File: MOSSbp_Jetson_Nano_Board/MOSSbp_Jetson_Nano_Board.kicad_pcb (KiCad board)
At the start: 2 copper layers, 0 parts

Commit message: Started PCB design
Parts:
- added C1: 4.7u, Capacitor_SMD:C_1206_3216Metric_Pad1.42x1.75mm_HandSolder, F.Cu at (122.5, 98.3)
- added C10: 4.7u, Capacitor_SMD:C_1206_3216Metric_Pad1.42x1.75mm_HandSolder, F.Cu at (132.2, 98.2)
- added C11: 2.2u, Capacitor_SMD:C_0603_1608Metric_Pad1.05x0.95mm_HandSolder, F.Cu at (169.0, 114.0)
- added C12: 0.1u, Capacitor_SMD:C_0603_1608Metric_Pad1.05x0.95mm_HandSolder, F.Cu at (129.4, 95.5)
- added C13: 330u, Capacitor_SMD:CP_Elec_8x10, F.Cu at (166.2, 69.0)
- added C2: 4.7u, Capacitor_SMD:C_1206_3216Metric_Pad1.42x1.75mm_HandSolder, F.Cu at (144.0, 98.5)
- added C3: 220u, Capacitor_SMD:CP_Elec_8x10.5, F.Cu at (125.0, 81.4)
- added C4: 10u, Capacitor_SMD:C_1206_3216Metric_Pad1.42x1.75mm_HandSolder, F.Cu at (131.4, 81.4)
- added C5: 0.1u, Capacitor_SMD:C_0603_1608Metric_Pad1.05x0.95mm_HandSolder, F.Cu at (119.6, 95.2)
- added C6: 0.1u, Capacitor_SMD:C_0603_1608Metric_Pad1.05x0.95mm_HandSolder, F.Cu at (140.9, 95.8)
- added C7: 22n, Capacitor_SMD:C_0603_1608Metric_Pad1.05x0.95mm_HandSolder, F.Cu at (141.6, 79.7)
- added C8: 0.1u, Capacitor_SMD:C_0603_1608Metric_Pad1.05x0.95mm_HandSolder, F.Cu at (136.2, 76.3)
- added C9: 47u, Capacitor_SMD:C_2220_5650Metric_Pad1.97x5.40mm_HandSolder, F.Cu at (135.2, 90.2)
- added D1: D, Diode_SMD:D_SOD-123, F.Cu at (119.3, 110.5)
- added D2: D, Diode_SMD:D_SOD-123, F.Cu at (133.7, 110.5)
- added D3: PMEG4030EP, Diode_SMD:D_SOD-128, F.Cu at (144.1, 79.8)
- added D4: D, Diode_SMD:D_SOD-123, F.Cu at (126.7, 110.5)
- added J1: 24V, TerminalBlock_Phoenix:TerminalBlock_Phoenix_MKDS-1,5-2_1x02_P5.00mm_Horizontal, F.Cu at (138.0, 68.2)
- added J2: Circulation Fan, Connector_JST:JST_GH_BM02B-GHS-TBT_1x02-1MP_P1.25mm_Vertical, F.Cu at (119.5, 115.1)
- added J3: CO2, Connector_JST:JST_GH_BM02B-GHS-TBT_1x02-1MP_P1.25mm_Vertical, F.Cu at (133.5, 115.1)
- added J4: Water Pump PWM, Connector_JST:JST_GH_BM02B-GHS-TBT_1x02-1MP_P1.25mm_Vertical, F.Cu at (140.5, 115.1)
- added J5: Vent Fan, Connector_JST:JST_GH_BM02B-GHS-TBT_1x02-1MP_P1.25mm_Vertical, F.Cu at (126.5, 115.1)
- added J6: Water Pump, Connector_JST:JST_XH_B2B-XH-AM_1x02_P2.50mm_Vertical, F.Cu at (145.5, 68.8)
- added J7: I2C, Connector_JST:JST_GH_BM04B-GHS-TBT_1x04-1MP_P1.25mm_Vertical, F.Cu at (156.3, 70.4)
- added J8: Jetson_Nano_Dev, Connector_PinHeader_2.54mm:PinHeader_2x20_P2.54mm_Vertical, F.Cu at (174.5, 68.7)
- added L1: 8.2u, RG_footprints:SRN8040-8R2Y, F.Cu at (142.5, 90.2)
- added Q1: DMN3404L, Package_TO_SOT_SMD:SOT-23, F.Cu at (119.5, 103.5)
- added Q2: DMN3404L, Package_TO_SOT_SMD:SOT-23, F.Cu at (141.2, 104.0)
- added Q3: BSS138, Package_TO_SOT_SMD:SOT-23, F.Cu at (143.1, 109.0)
- added Q4: DMN3404L, Package_TO_SOT_SMD:SOT-23, F.Cu at (129.2, 103.8)
- added R1: 23.7k, Resistor_SMD:R_0603_1608Metric_Pad1.05x0.95mm_HandSolder, F.Cu at (136.2, 83.9)
- added R10: 4.7k, Resistor_SMD:R_0603_1608Metric_Pad1.05x0.95mm_HandSolder, F.Cu at (139.0, 109.0)
- added R2: 4.7k, Resistor_SMD:R_0603_1608Metric_Pad1.05x0.95mm_HandSolder, F.Cu at (117.0, 98.1)
- added R3: 4.7k, Resistor_SMD:R_0603_1608Metric_Pad1.05x0.95mm_HandSolder, F.Cu at (137.8, 98.8)
- added R4: 100k, Resistor_SMD:R_0603_1608Metric_Pad1.05x0.95mm_HandSolder, F.Cu at (130.1, 88.6)
- added R5: 6.49k, Resistor_SMD:R_0603_1608Metric_Pad1.05x0.95mm_HandSolder, F.Cu at (130.1, 91.9)
- added R6: 10k, Resistor_SMD:R_0603_1608Metric_Pad1.05x0.95mm_HandSolder, F.Cu at (145.5, 109.1)
- added R7: 10k, Resistor_SMD:R_0603_1608Metric_Pad1.05x0.95mm_HandSolder, F.Cu at (140.5, 109.1)
- added R8: 4.7k, Resistor_SMD:R_0603_1608Metric_Pad1.05x0.95mm_HandSolder, F.Cu at (126.5, 98.4)
- added R9: 21k, Resistor_SMD:R_0603_1608Metric_Pad1.05x0.95mm_HandSolder, F.Cu at (165.1, 114.0)
- added U1: MIC4416, Package_TO_SOT_SMD:SOT-143, F.Cu at (119.5, 98.2)
- added U2: MIC4416, Package_TO_SOT_SMD:SOT-143, F.Cu at (140.8, 98.7)
- added U3: LMR14020, Package_SO:SOIC-8-1EP_3.9x4.9mm_P1.27mm_EP2.41x3.3mm, F.Cu at (136.5, 80.1)
- added U4: PTN78020WAH, RG_footprints:PTN78020WAH, F.Cu at (160.4, 94.5)
- added U5: MIC4416, Package_TO_SOT_SMD:SOT-143, F.Cu at (129.2, 98.5)
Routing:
- added copper zone on B.Cu, net GND
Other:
- board outline added: 65 x 60 mm

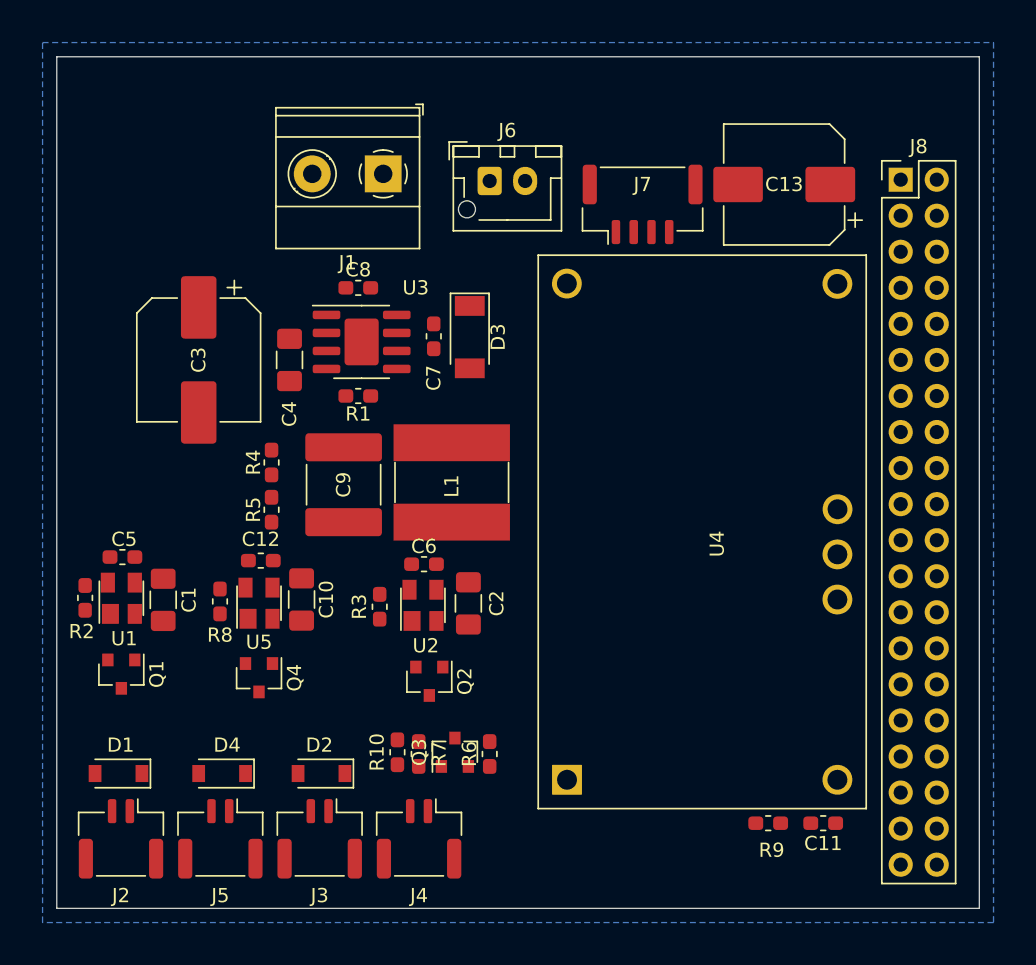
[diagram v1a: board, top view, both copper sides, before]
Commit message: Finished PCB routing
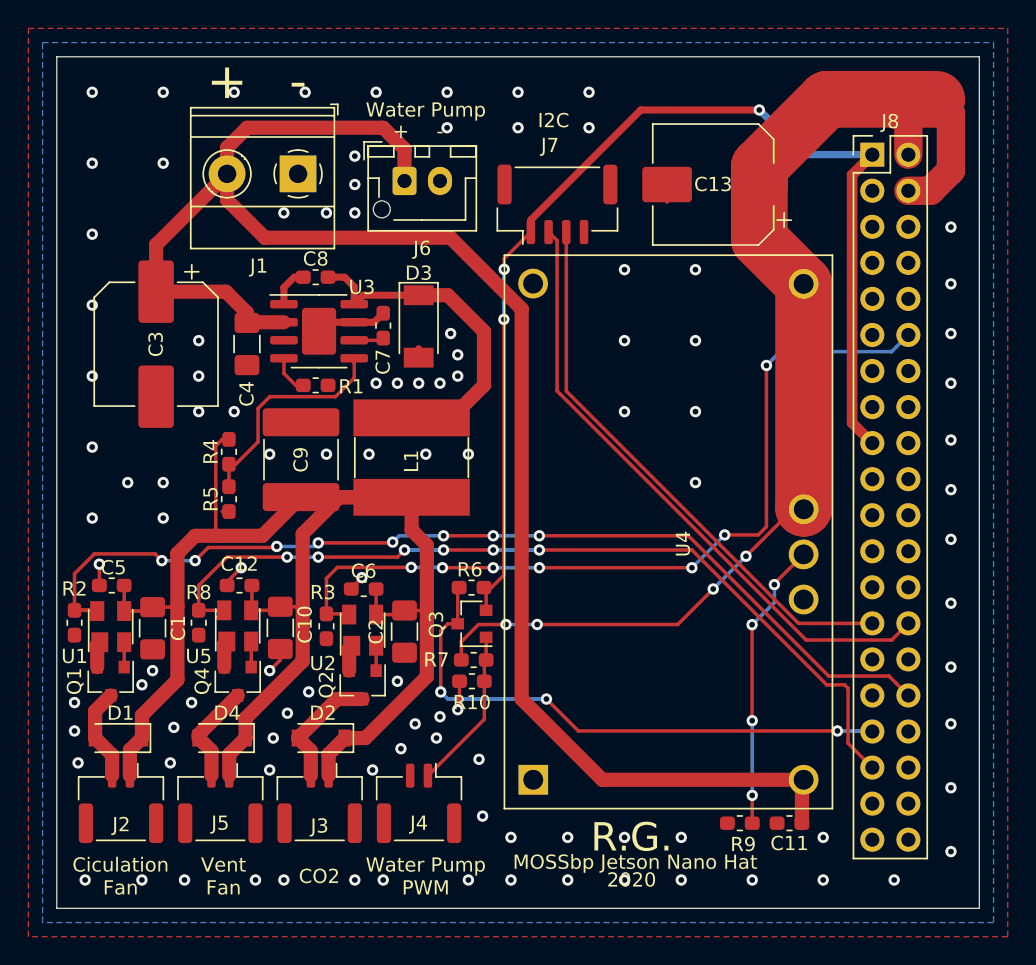
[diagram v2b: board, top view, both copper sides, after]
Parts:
- moved R6 11.8 mm to (144.2, 97.4), turned to 180 degrees
- moved Q3 9.13 mm to (144.2, 100.0), turned to 180 degrees
- moved R7 7.68 mm to (144.4, 102.5), turned to 0 degrees
- moved R10 7.25 mm to (144.2, 104.0), turned to 180 degrees
- moved J1 6.00 mm to (132.0, 68.2)
- moved J6 6.00 mm to (139.5, 68.8)
- moved J7 6.00 mm to (150.3, 70.4)
- moved C13 5.00 mm to (161.2, 69.0)
- moved C2 4.92 mm to (139.5, 100.5), turned to 270 degrees
- moved Q2 4.71 mm to (136.6, 104.2)
- moved C6 4.60 mm to (136.6, 97.5)
- moved U2 4.60 mm to (136.6, 100.4)
- moved R3 3.99 mm to (134.0, 100.1), turned to 270 degrees
- moved D3 3.68 mm to (140.5, 79.0)
- moved C7 3.64 mm to (138.0, 78.9)
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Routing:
- net +24V: track 0.00 -> 117.1 mm
- net +12V: track 0.00 -> 112.5 mm
- net +5V: track 0.00 -> 82.8 mm, vias 0 -> 4
- net +3V3: track 0.00 -> 79.3 mm, vias 0 -> 3
- net /CF_CTRL: track 0.00 -> 70.4 mm, vias 0 -> 8
- net /VF_CTRL: track 0.00 -> 61.4 mm, vias 0 -> 6
- net /CO2_CTRL: track 0.00 -> 59.1 mm, vias 0 -> 7
- net /I2C1_SCL: track 0.00 -> 44.0 mm
- net /WP_PWM: track 0.00 -> 39.9 mm, vias 0 -> 3
- net /I2C1_SDA: track 0.00 -> 39.5 mm
- net Net-(C8-Pad1): track 0.00 -> 24.0 mm
- net GND: track 0.00 -> 22.0 mm, vias 0 -> 106
- net Net-(R9-Pad2): track 0.00 -> 20.4 mm, vias 0 -> 4
- net Net-(R4-Pad2): track 0.00 -> 15.7 mm
- net Net-(J4-Pad1): track 0.00 -> 11.4 mm
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- added copper zone on F.Cu, net GND
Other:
- board text added: "+"
- board text added: "-"
- board text added: "2020"
- board text added: "CO2"
- board text added: "Ciculation Fan"
- board text added: "I2C"
- board text added: "MOSSbp Jetson Nano Hat"
- board text added: "R.G."
- board text added: "Vent Fan"
- board text added: "Water Pump"
- board text added: "Water Pump PWM"

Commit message: Adding temperature sensors
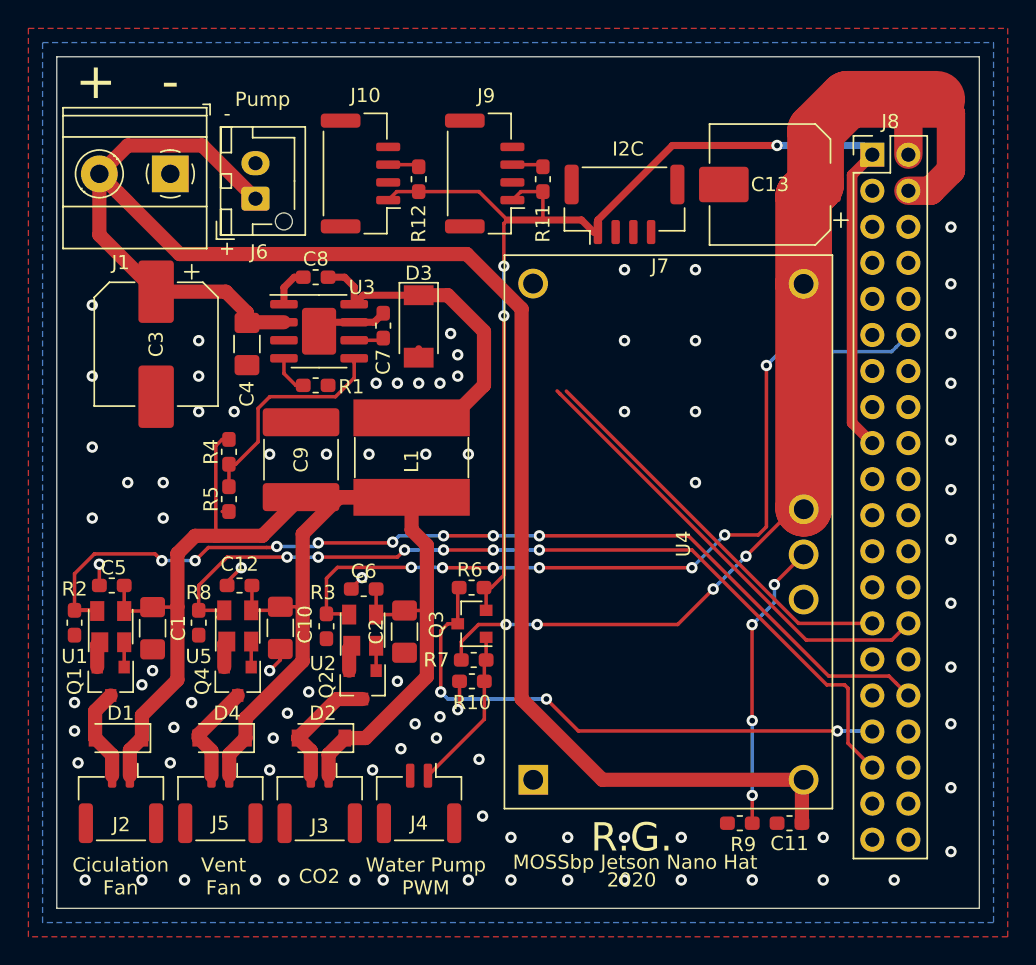
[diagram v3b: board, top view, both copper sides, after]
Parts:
- added J10: Temp2, Connector_JST:JST_GH_BM04B-GHS-TBT_1x04-1MP_P1.25mm_Vertical, F.Cu at (136.4, 68.2)
- added J9: Temp1, Connector_JST:JST_GH_BM04B-GHS-TBT_1x04-1MP_P1.25mm_Vertical, F.Cu at (145.2, 68.2)
- added R11: 4.7k, Resistor_SMD:R_0603_1608Metric_Pad1.05x0.95mm_HandSolder, F.Cu at (149.2, 68.6)
- added R12: 4.7k, Resistor_SMD:R_0603_1608Metric_Pad1.05x0.95mm_HandSolder, F.Cu at (140.5, 68.6)
- moved J6 10.6 mm to (129.0, 70.0), turned to 90 degrees
- moved J1 9.00 mm to (123.0, 68.2)
- moved J7 4.72 mm to (155.0, 70.4)
- moved C13 4.00 mm to (165.2, 69.0)
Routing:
- net +3V3: track 79.3 -> 93.3 mm
- net /I2C1_SCL: track 44.0 -> 32.5 mm
- net /I2C1_SDA: track 39.5 -> 28.3 mm
- net +24V: track 117.1 -> 121.2 mm
- net +5V: track 82.8 -> 79.4 mm
- net /Temp2_I: track 0.00 -> 2.21 mm
- net /Temp1_I: track 0.00 -> 2.21 mm
- net GND: track 22.0 -> 20.7 mm, vias 106 -> 87
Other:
- board text added: "Pump"
- board text removed: "Water Pump"

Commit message: Finished adding temp sensors
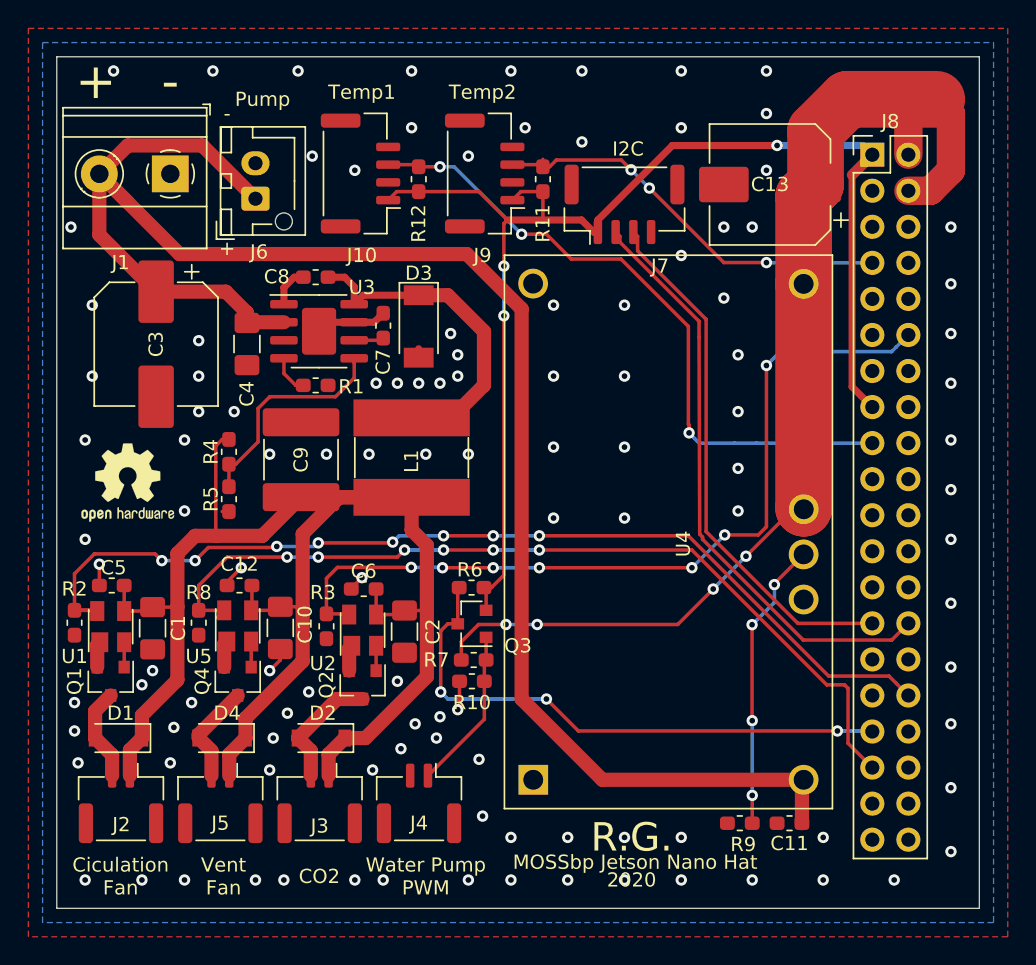
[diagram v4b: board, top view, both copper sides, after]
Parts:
- added REF**: OSHW-Logo2_7.3x6mm_SilkScreen, Symbol:OSHW-Logo2_7.3x6mm_SilkScreen, F.Cu at (120.0, 90.0)
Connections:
- J8 pad 15: (no net) -> +3V3
- J8 pad 17: +3V3 -> /Temp2_I
- J8 pad 7: (no net) -> /Temp1_I
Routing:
- net /Temp2_I: track 2.21 -> 46.6 mm, vias 0 -> 3
- net /Temp1_I: track 2.21 -> 29.1 mm, vias 0 -> 3
- net /I2C1_SCL: track 32.5 -> 42.1 mm
- net /I2C1_SDA: track 28.3 -> 37.6 mm
- net +3V3: track 93.3 -> 90.7 mm
- net GND: vias 87 -> 113
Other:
- board text added: "Temp1"
- board text added: "Temp2"
